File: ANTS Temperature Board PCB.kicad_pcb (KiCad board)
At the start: 2 copper layers, 50 x 70 mm, 14 parts, among them J1 1751251, J3 EBWA-02-A, J5 EBWA-02-A, J6 B2B-XH-A, J7 B2B-XH-A, Q1 IRLZ34N, U1 RASPBERRY_PI_PICO

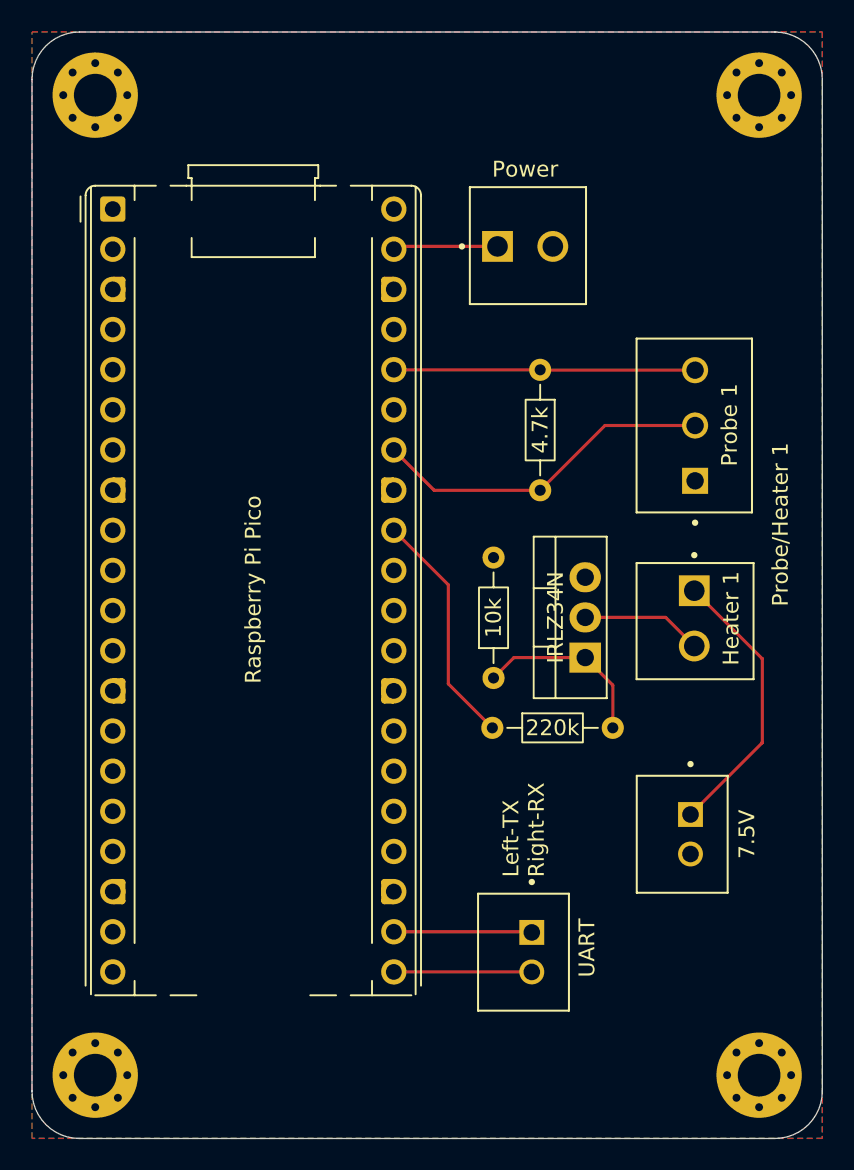
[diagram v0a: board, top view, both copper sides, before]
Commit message: Updated mounting holes to M3.
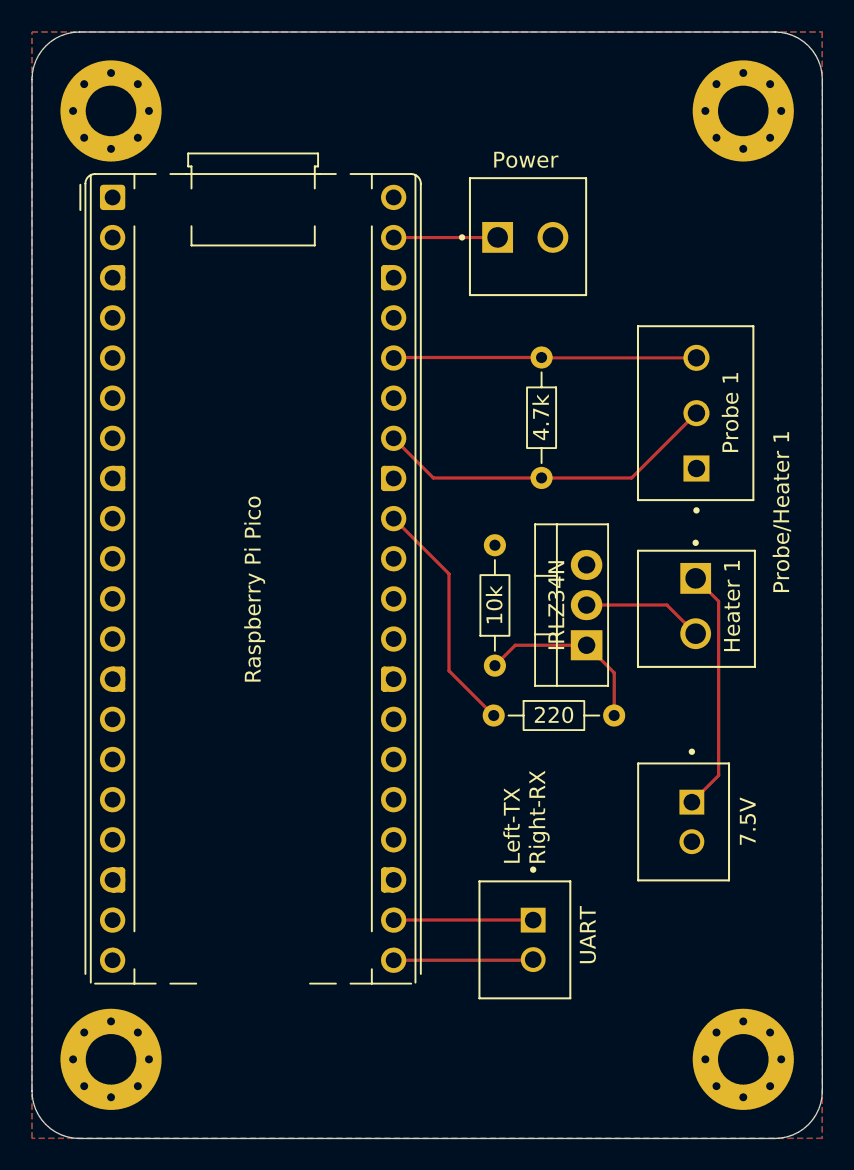
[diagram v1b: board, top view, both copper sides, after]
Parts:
- H1, H2, H3, H4: footprint MountingHole:MountingHole_2.7mm_M2.5_Pad_Via -> MountingHole:MountingHole_3.2mm_M3_Pad_Via
- moved H4 1.42 mm to (113.3, 91.7)
- moved H2 1.41 mm to (113.3, 31.7)
- moved H3 1.41 mm to (73.3, 91.7)
- moved H1 1.41 mm to (73.3, 31.7)
- moved J1 0.78 mm to (113.9, 56.3)
- moved J3 0.78 mm to (110.3, 63.0)
- moved J6 0.78 mm to (99.5, 84.1)
- moved R1 0.78 mm to (97.6, 66.8)
- moved R7 0.78 mm to (97.5, 69.9)
- moved Q1 0.78 mm to (103.4, 65.5)
- moved R5 0.78 mm to (100.5, 47.3)
- moved J7 0.78 mm to (109.5, 76.7)
- moved U1 0.74 mm to (73.4, 37.2)
- moved J5 0.57 mm to (99.5, 39.7)
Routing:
- net +7.5V: track 17.8 -> 15.5 mm
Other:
- board text added: "220"
- board text removed: "220k"

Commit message: Updated board M2.5 screws again
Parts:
- H1, H2, H3, H4: footprint MountingHole:MountingHole_3.2mm_M3_Pad_Via -> MountingHole:MountingHole_2.7mm_M2.5_Pad_Via

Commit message: Fixed small error with difference in footprints.
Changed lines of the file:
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@@
 			(at 0 -3.65 0)
 			(layer "F.SilkS")
+			(hide yes)
 			(effects
 				(font
@@
 			(at 0 -3.65 0)
 			(layer "F.SilkS")
+			(hide yes)
 			(effects
 				(font
@@
 			(at 0 -3.65 0)
 			(layer "F.SilkS")
+			(hide yes)
 			(effects
 				(font
@@
 			(at 0 -3.65 0)
 			(layer "F.SilkS")
+			(hide yes)
 			(effects
 				(font
@@
 		(start 111.74 62.725)
 		(end 110.286675 61.271675)
-		(width 0.2)
+		(width 0.5)
 		(layer "F.Cu")
 		(net "+7.5V")
@@
 		(start 110.0475 75.43)
 		(end 111.74 73.7375)
-		(width 0.2)
+		(width 0.5)
 		(layer "F.Cu")
 		(net "+7.5V")
@@
 		(start 111.74 73.7375)
 		(end 111.74 62.725)
-		(width 0.2)
+		(width 0.5)
 		(layer "F.Cu")
 		(net "+7.5V")
@@
 		)
 		(min_thickness 0.25)
-		(fill yes
+		(fill
 			(thermal_gap 0.5)
 			(thermal_bridge_width 0.5)
@@
 		)
 		(min_thickness 0.25)
-		(fill yes
+		(fill
 			(thermal_gap 0.5)
 			(thermal_bridge_width 0.5)
